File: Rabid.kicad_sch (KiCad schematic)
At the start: 219 parts, among them J1 USB Header, SW1 Esc, SW10 A, SW100 Unused, SW101 Unused, SW102 →, SW11 Z, SW12 LMeta, SW13 F1, SW14 2, SW15 W, SW16 S, SW17 X, SW18 LAlt, SW19 F2, SW2 Tilde, SW20 3, SW21 E, SW22 D, SW23 C, SW24 Unused, SW25 F3, SW26 4, SW27 R, SW28 F, SW29 V, SW3 Tab, SW30 Unused, SW31 F4, SW32 5, SW33 T, SW34 G, SW35 B, SW36 Unused, SW37 F5, SW38 6, SW39 Y, SW4 CapsLk, SW40 H, SW41 N, SW42 Space, SW43 F6, SW44 7, SW45 U, SW46 J, SW47 M, SW48 Unused, SW49 F7, SW5 LShift, SW50 8, SW51 I, SW52 K, SW53 ,, SW54 Unused, SW55 F8, SW56 9, SW57 O, SW58 L, SW59 ., SW6 LCtrl, SW60 Unused, SW61 F9, SW62 0, SW63 P, SW64 ;, SW65 /, SW66 AltGr, SW67 F10, SW68 -, SW69 [, SW7 Unused, SW70 ", SW71 RShift, SW72 RMeta, SW73 F11, SW74 =, SW75 ], SW76 ↲, SW77 Unused, SW78 Fn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

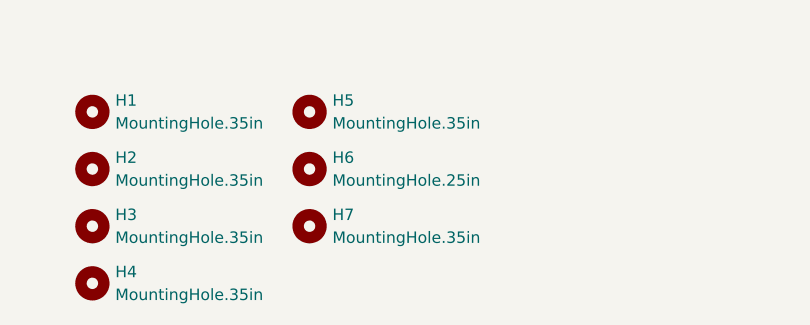
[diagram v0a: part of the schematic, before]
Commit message: Changed dimensions, moved function row up, added mounting hole.
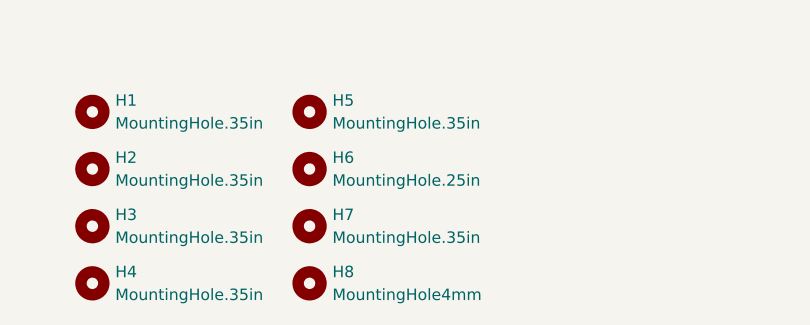
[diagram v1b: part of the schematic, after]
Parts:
- added H8: MountingHole4mm, MountingHole:MountingHole_4mm, symbol Mechanical:MountingHole
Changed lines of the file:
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@@
     (pin "2")
+  )
+  (symbol (lib_id "Mechanical:MountingHole") (at 278.13 280.67 0) (unit 1)
+    (in_bom yes) (on_board yes) (fields_autoplaced)
+    (property "Reference" "H8" (id 0) (at 280.67 279.3999 0)
+      (effects (font (size 1.27 1.27)) (justify left))
+    )
+    (property "Value" "MountingHole4mm" (id 1) (at 280.67 281.9399 0)
+      (effects (font (size 1.27 1.27)) (justify left))
+    )
+    (property "Footprint" "MountingHole:MountingHole_4mm" (id 2) (at 278.13 280.67 0)
+      (effects (font (size 1.27 1.27)) hide)
+    )
+    (property "Datasheet" "~" (id 3) (at 278.13 280.67 0)
+      (effects (font (size 1.27 1.27)) hide)
+    )
   )
   (symbol (lib_id "Switch:SW_Push") (at 190.5 92.71 0) (unit 1)
@@
       (reference "H7") (unit 1) (value "MountingHole.35in") (footprint "RabidKeyboard:MountingHole_.35in")
     )
+    (path "/daf18d95-a29d-445d-9e50-3ca1c1c87614"
+      (reference "H8") (unit 1) (value "MountingHole4mm") (footprint "MountingHole:MountingHole_4mm")
+    )
     (path "/bbea82d0-8c64-4c6e-81d8-7d16f5942bd3"

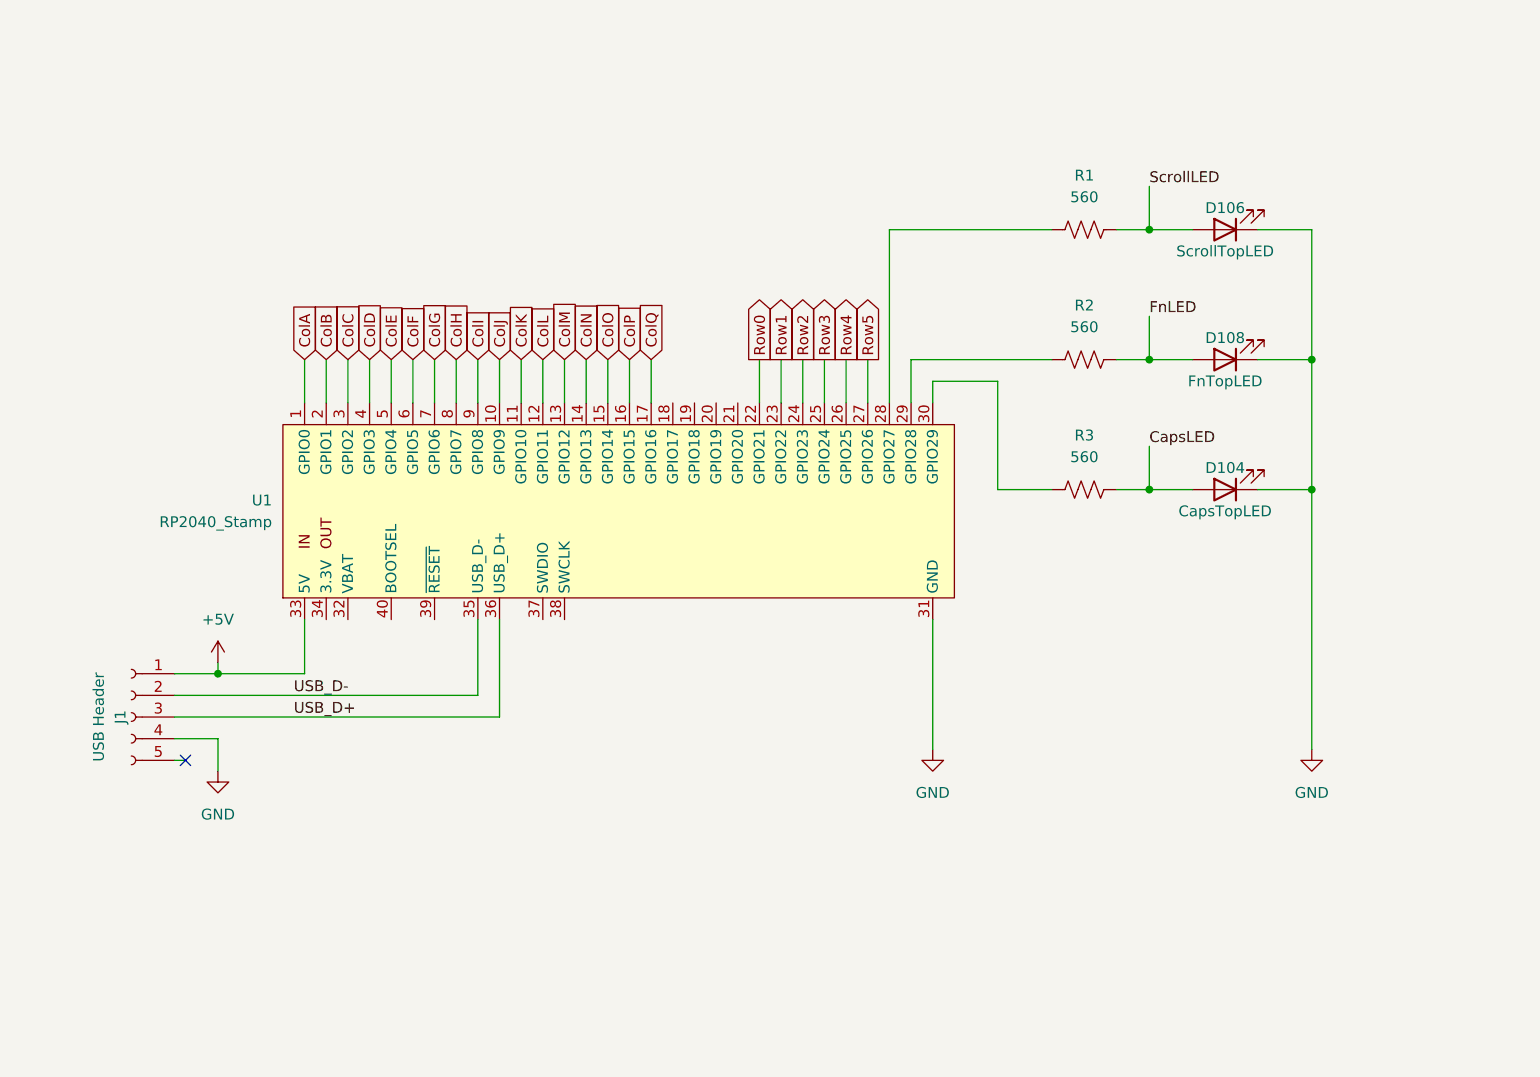
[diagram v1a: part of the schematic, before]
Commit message: Add GPIO/Debug header, bootsel, and reset switch.
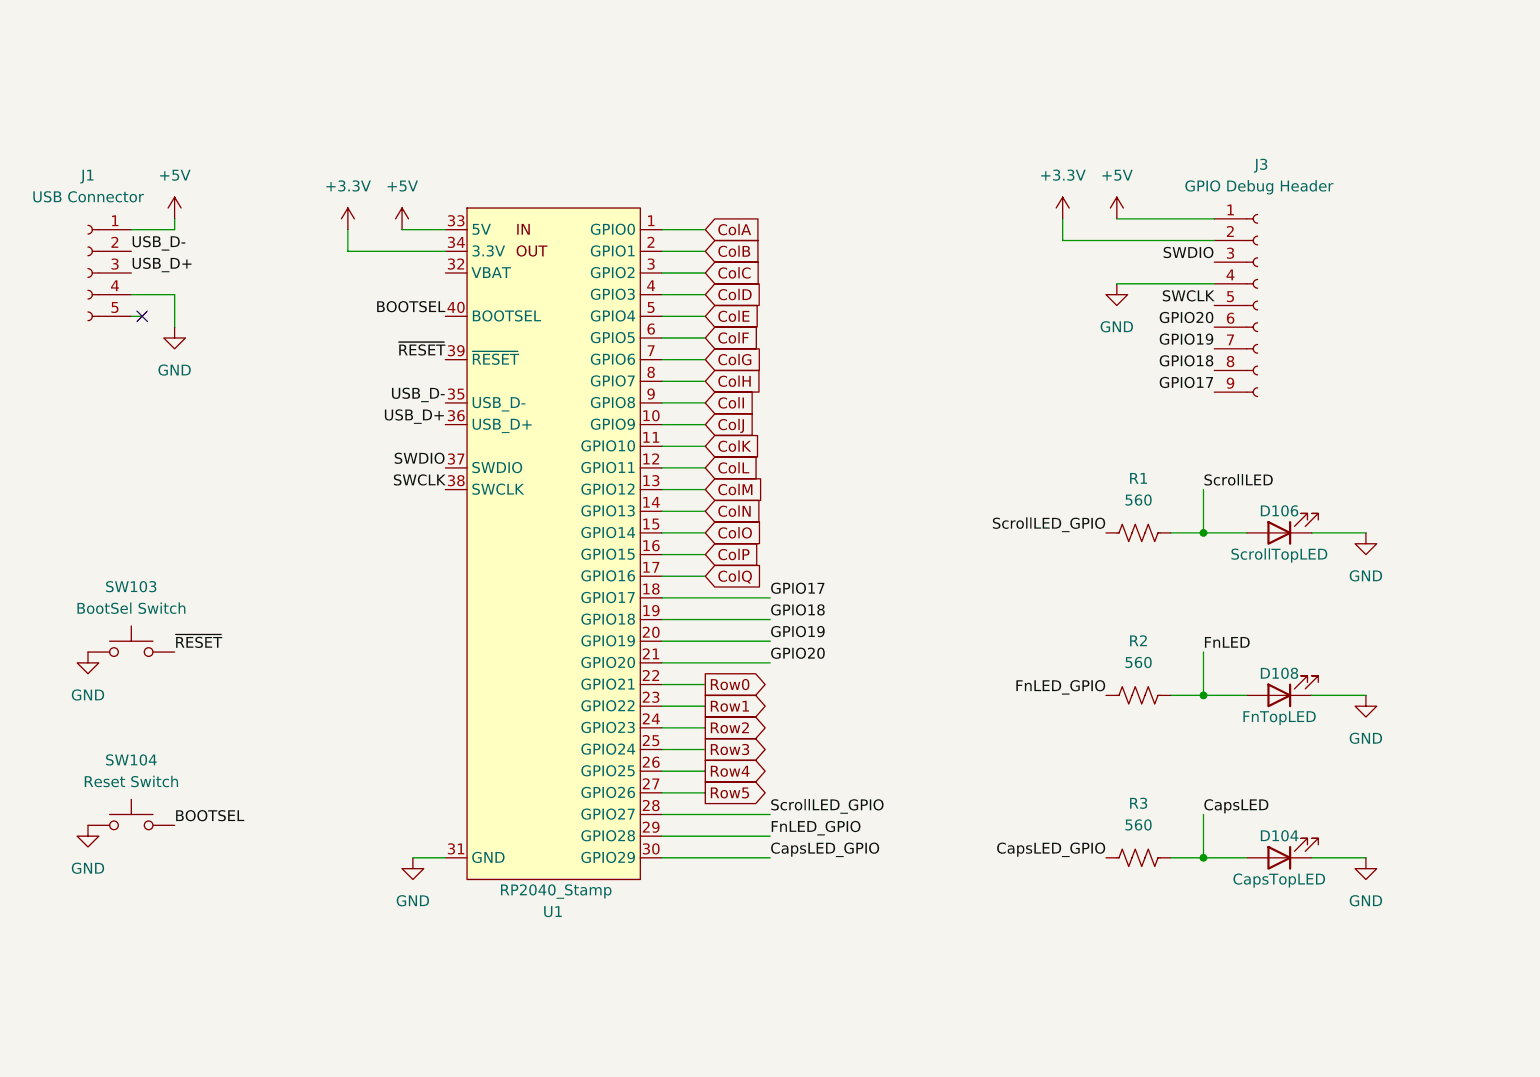
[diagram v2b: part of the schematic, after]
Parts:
- added J3: GPIO Debug Header, Connector_PinHeader_2.54mm:PinHeader_1x09_P2.54mm_Horizontal, symbol Connector:Conn_01x09_Female
- added SW103: BootSel Switch, Button_Switch_THT:SW_PUSH_6mm, symbol Switch:SW_Push
- added SW104: Reset Switch, Button_Switch_THT:SW_PUSH_6mm, symbol Switch:SW_Push
- J1: value USB Header -> USB Connector; footprint Connector_JST:JST_PH_S5B-PH-SM4-TB_1x05-1MP_P2.00mm_Horizontal -> Connector_JST:JST_PH_S5B-PH-K_1x05_P2.00mm_Horizontal
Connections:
- net +5V: now also J3.1 (Pin_1)
- net GND: now also J3.4 (Pin_4), SW103.1, SW104.1
- net FnLED_GPIO: now reaches R2.1, U1.29 (GPIO28)
- net GPIO17: now reaches U1.18 (GPIO17)
- net GPIO17: now also J3.9 (Pin_9)
- net GPIO18: now reaches U1.19 (GPIO18)
- net GPIO18: now also J3.8 (Pin_8)
- net GPIO19: now reaches U1.20 (GPIO19)
- net GPIO19: now also J3.7 (Pin_7)
- net GPIO20: now reaches U1.21 (GPIO20)
- net GPIO20: now also J3.6 (Pin_6)
- net ScrollLED_GPIO: now reaches R1.1, U1.28 (GPIO27)
- net CapsLED_GPIO: now reaches R3.1, U1.30 (GPIO29)
- net +3V3: now reaches U1.34 (3.3V)
- net +3V3: now also J3.2 (Pin_2)
- net SWDIO: now reaches U1.37 (SWDIO)
- net SWDIO: now also J3.3 (Pin_3)
- net SWCLK: now reaches U1.38 (SWCLK)
- net SWCLK: now also J3.5 (Pin_5)
- net ~{RESET}: now reaches U1.39 (~{RESET})
- net ~{RESET}: now also SW103.2
- net BOOTSEL: now reaches U1.40 (BOOTSEL)
- net BOOTSEL: now also SW104.2
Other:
- moved on the sheet: D104, D106, D108, J1, R1, R2, R3, U1

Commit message: Add project title/author/revision/url to silkscreen.
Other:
- company: (none) -> ${COMPANY}
- title: RabidKeyboard -> ${TITLE}
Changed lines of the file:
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@@
   (paper "A3")
   (title_block
-    (title "RabidKeyboard")
+    (title "${TITLE}")
+    (rev "${REVISION}")
+    (company "${COMPANY}")
   )
   (junction (at 182.88 92.71) (diameter 0) (color 0 0 0 0)

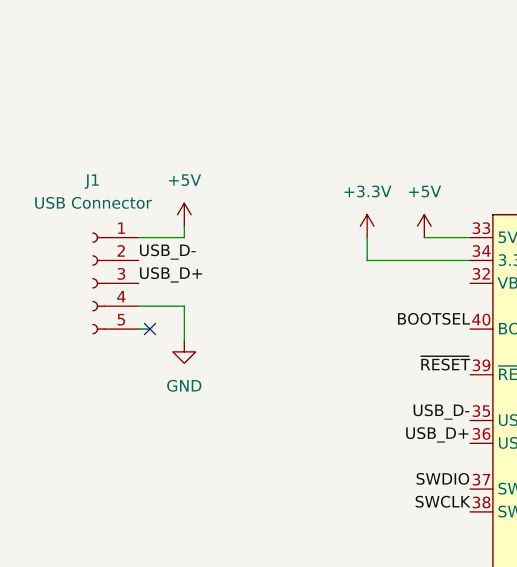
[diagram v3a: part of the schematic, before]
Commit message: Flip USB pinout to match original PCB.
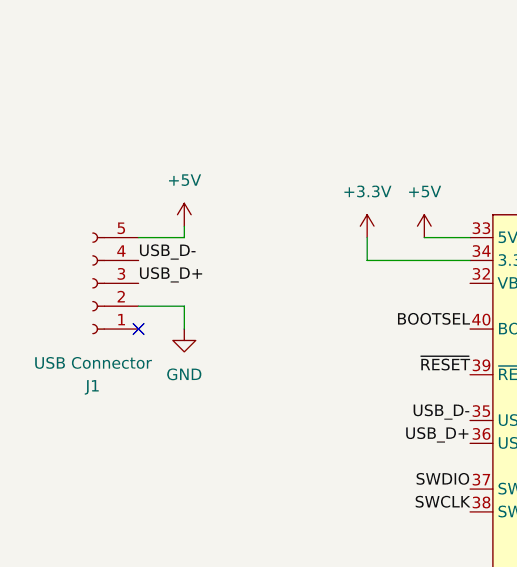
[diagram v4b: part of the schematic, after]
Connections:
- net +5V: now also J1.5 (Pin_5); no longer J1.1 (Pin_1)
- net GND: now also J1.2 (Pin_2); no longer J1.4 (Pin_4)
- net USB_D-: now also J1.4 (Pin_4); no longer J1.2 (Pin_2)
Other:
- moved on the sheet: J1
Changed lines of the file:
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@@
   (junction (at 226.06 60.96) (diameter 0) (color 0 0 0 0)
   )
-  (no_connect (at 34.29 193.04))
+  (no_connect (at 33.02 193.04))
   (wire (pts (xy 185.42 35.56) (xy 185.42 41.91))
     (stroke (width 0) (type default) (color 0 0 0 0))
@@
     (stroke (width 0) (type default) (color 0 0 0 0))
   )
-  (wire (pts (xy 33.02 190.5) (xy 38.1 190.5))
-    (stroke (width 0) (type default) (color 0 0 0 0))
-  )
   (wire (pts (xy 43.18 22.86) (xy 43.18 29.21))
     (stroke (width 0) (type default) (color 0 0 0 0))
@@
     (stroke (width 0) (type default) (color 0 0 0 0))
   )
-  (wire (pts (xy 38.1 181.61) (xy 38.1 182.88))
-    (stroke (width 0) (type default) (color 0 0 0 0))
-  )
   (wire (pts (xy 327.66 60.96) (xy 347.98 60.96))
     (stroke (width 0) (type default) (color 0 0 0 0))
@@
     (stroke (width 0) (type default) (color 0 0 0 0))
   )
-  (wire (pts (xy 33.02 182.88) (xy 38.1 182.88))
-    (stroke (width 0) (type default) (color 0 0 0 0))
-  )
   (wire (pts (xy 124.46 86.36) (xy 124.46 92.71))
     (stroke (width 0) (type default) (color 0 0 0 0))
@@
     (stroke (width 0) (type default) (color 0 0 0 0))
   )
+  (wire (pts (xy 38.1 193.04) (xy 38.1 190.5))
+    (stroke (width 0) (type default) (color 0 0 0 0))
+  )
   (wire (pts (xy 100.33 238.76) (xy 95.25 238.76))
     (stroke (width 0) (type default) (color 0 0 0 0))
@@
     (stroke (width 0) (type default) (color 0 0 0 0))
   )
+  (wire (pts (xy 38.1 190.5) (xy 33.02 190.5))
+    (stroke (width 0) (type default) (color 0 0 0 0))
+  )
   (wire (pts (xy 124.46 35.56) (xy 124.46 41.91))
     (stroke (width 0) (type default) (color 0 0 0 0))
@@
     (stroke (width 0) (type default) (color 0 0 0 0))
   )
-  (wire (pts (xy 33.02 193.04) (xy 34.29 193.04))
-    (stroke (width 0) (type default) (color 0 0 0 0))
-  )
   (wire (pts (xy 165.1 73.66) (xy 165.1 80.01))
     (stroke (width 0) (type default) (color 0 0 0 0))
@@
     (stroke (width 0) (type default) (color 0 0 0 0))
   )
+  (wire (pts (xy 33.02 182.88) (xy 38.1 182.88))
+    (stroke (width 0) (type default) (color 0 0 0 0))
+  )
   (wire (pts (xy 203.2 92.71) (xy 203.2 99.06))
     (stroke (width 0) (type default) (color 0 0 0 0))
@@
     (stroke (width 0) (type default) (color 0 0 0 0))
   )
-  (wire (pts (xy 38.1 190.5) (xy 38.1 194.31))
-    (stroke (width 0) (type default) (color 0 0 0 0))
-  )
   (wire (pts (xy 63.5 86.36) (xy 63.5 92.71))
     (stroke (width 0) (type default) (color 0 0 0 0))
@@
     (stroke (width 0) (type default) (color 0 0 0 0))
   )
+  (wire (pts (xy 38.1 182.88) (xy 38.1 181.61))
+    (stroke (width 0) (type default) (color 0 0 0 0))
+  )
   (wire (pts (xy 154.94 218.44) (xy 158.75 218.44))
     (stroke (width 0) (type default) (color 0 0 0 0))
@@
     (pin "2")
   )
-  (symbol (lib_id "power:+5V") (at 38.1 181.61 0) (unit 1)
+  (symbol (lib_id "power:+5V") (at 38.1 181.61 0) (mirror y) (unit 1)
     (in_bom yes) (on_board yes) (fields_autoplaced)
     (property "Reference" "#PWR0101" (id 0) (at 38.1 185.42 0)
@@
     (pin "2")
   )
-  (symbol (lib_id "power:GND") (at 38.1 194.31 0) (unit 1)
+  (symbol (lib_id "power:GND") (at 38.1 193.04 0) (mirror y) (unit 1)
     (in_bom yes) (on_board yes) (fields_autoplaced)
-    (property "Reference" "#PWR01" (id 0) (at 38.1 200.66 0)
+    (property "Reference" "#PWR01" (id 0) (at 38.1 199.39 0)
       (effects (font (size 1.27 1.27)) hide)
     )
-    (property "Value" "GND" (id 1) (at 38.1 199.39 0))
-    (property "Footprint" "" (id 2) (at 38.1 194.31 0)
+    (property "Value" "GND" (id 1) (at 38.1 198.12 0))
+    (property "Footprint" "" (id 2) (at 38.1 193.04 0)
       (effects (font (size 1.27 1.27)) hide)
     )
-    (property "Datasheet" "" (id 3) (at 38.1 194.31 0)
+    (property "Datasheet" "" (id 3) (at 38.1 193.04 0)
       (effects (font (size 1.27 1.27)) hide)
     )
@@
     (pin "1")
   )
-  (symbol (lib_id "Connector:Conn_01x05_Female") (at 27.94 187.96 0) (mirror y) (unit 1)
+  (symbol (lib_id "Connector:Conn_01x05_Female") (at 27.94 187.96 180) (unit 1)
     (in_bom yes) (on_board yes)
-    (property "Reference" "J1" (id 0) (at 27.94 176.53 0))
-    (property "Value" "USB Connector" (id 1) (at 27.94 179.07 0))
+    (property "Reference" "J1" (id 0) (at 27.94 199.39 0))
+    (property "Value" "USB Connector" (id 1) (at 27.94 196.85 0))
     (property "Footprint" "Connector_JST:JST_PH_S5B-PH-K_1x05_P2.00mm_Horizontal" (id 2) (at 27.94 187.96 0)
       (effects (font (size 1.27 1.27)) hide)
